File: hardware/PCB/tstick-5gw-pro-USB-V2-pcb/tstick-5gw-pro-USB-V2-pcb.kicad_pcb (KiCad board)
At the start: 4 copper layers, 53.3 x 25.4 mm, 62 parts, among them J1 USB_C_Receptacle_USB2.0, Q1 BSS138, Q2 BSS138, Q3 BSS138, SW1 B3U-1000P, SW2 B3U-1000P, U1 USBLC6-2P6, U2 MCP73871, U3 NCP167AMX330TBG, U4 NCP167AMX180TBG

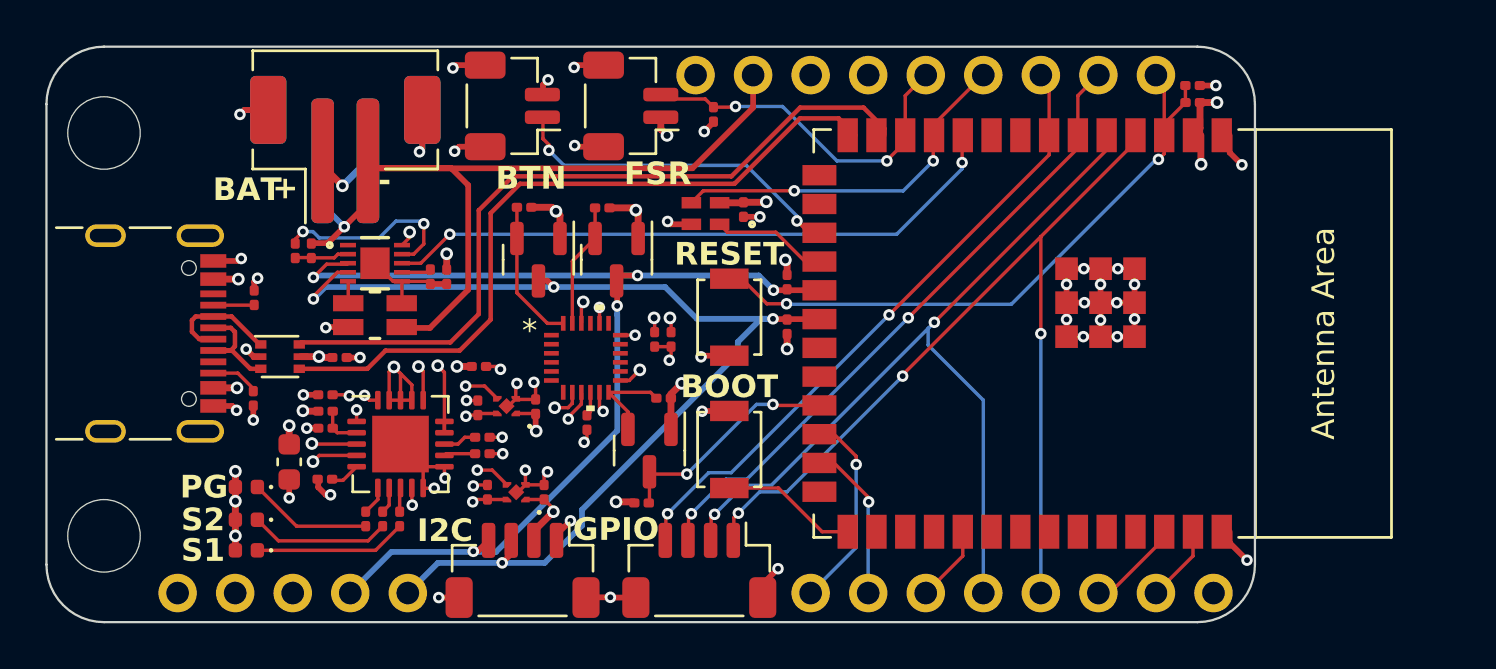
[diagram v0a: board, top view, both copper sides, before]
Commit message: removed neopixel, changed BOM, added simple status LEDs
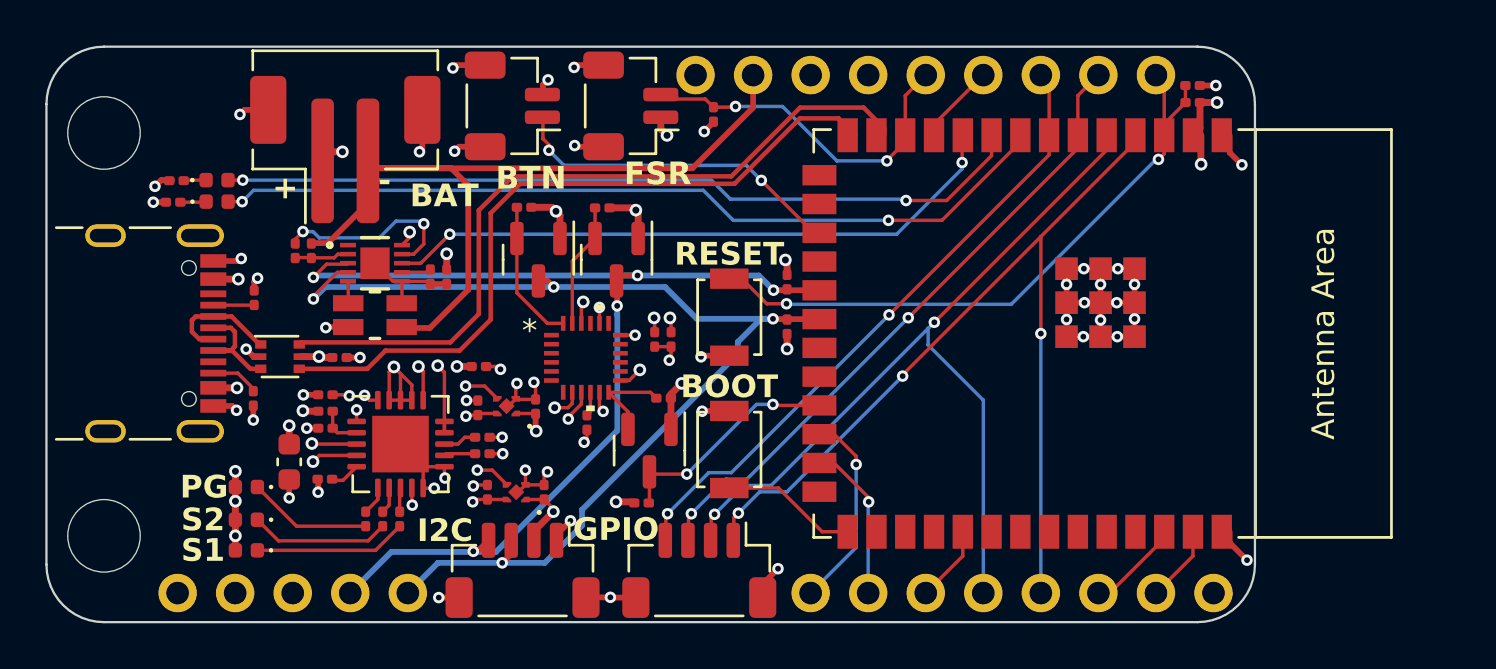
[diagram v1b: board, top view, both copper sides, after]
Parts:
- removed BT2: JST-PH-1x02-2.000mm, Connector_JST:JST_PH_B2B-PH-SM4-TB_1x02-1MP_P2.00mm_Vertical
- removed C13: 0.1uF, Capacitor_SMD:C_0201_0603Metric
- removed PWLED1: SK6805-E-J, neopixel-1515-footprints:4492_ADA
- added R10: 1k, Resistor_SMD:R_0201_0603Metric, F.Cu at (98.5, 54.2)
- added R8: 1k, Resistor_SMD:R_0201_0603Metric, F.Cu at (98.3, 55.1)
- added STATLED1: LED, LED_SMD:LED_0402_1005Metric, F.Cu at (100.2, 55.1)
- added STATLED2: LED, LED_SMD:LED_0402_1005Metric, F.Cu at (100.2, 54.1)
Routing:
- net /IO15: track 0.00 -> 37.5 mm, vias 0 -> 2
- net /IO16: track 0.00 -> 35.8 mm, vias 0 -> 2
- net /IO18: track 16.1 -> 3.56 mm, vias 2 -> 0
- net /IO10: track 6.41 -> 0.00 mm
- net GND: track 72.6 -> 68.5 mm
- net -BATT: track 40.4 -> 37.1 mm, vias 1 -> 0
- net +3V3: track 11.9 -> 9.83 mm, vias 8 -> 7
- net +BATT: track 10.2 -> 8.23 mm
- net Net-(STATLED1-K): track 0.00 -> 1.13 mm
- net Net-(STATLED2-K): track 0.00 -> 0.86 mm
- net /IO9: track 15.5 -> 14.8 mm

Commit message: removed unused fuel gauge thresholds, added jab thresholds
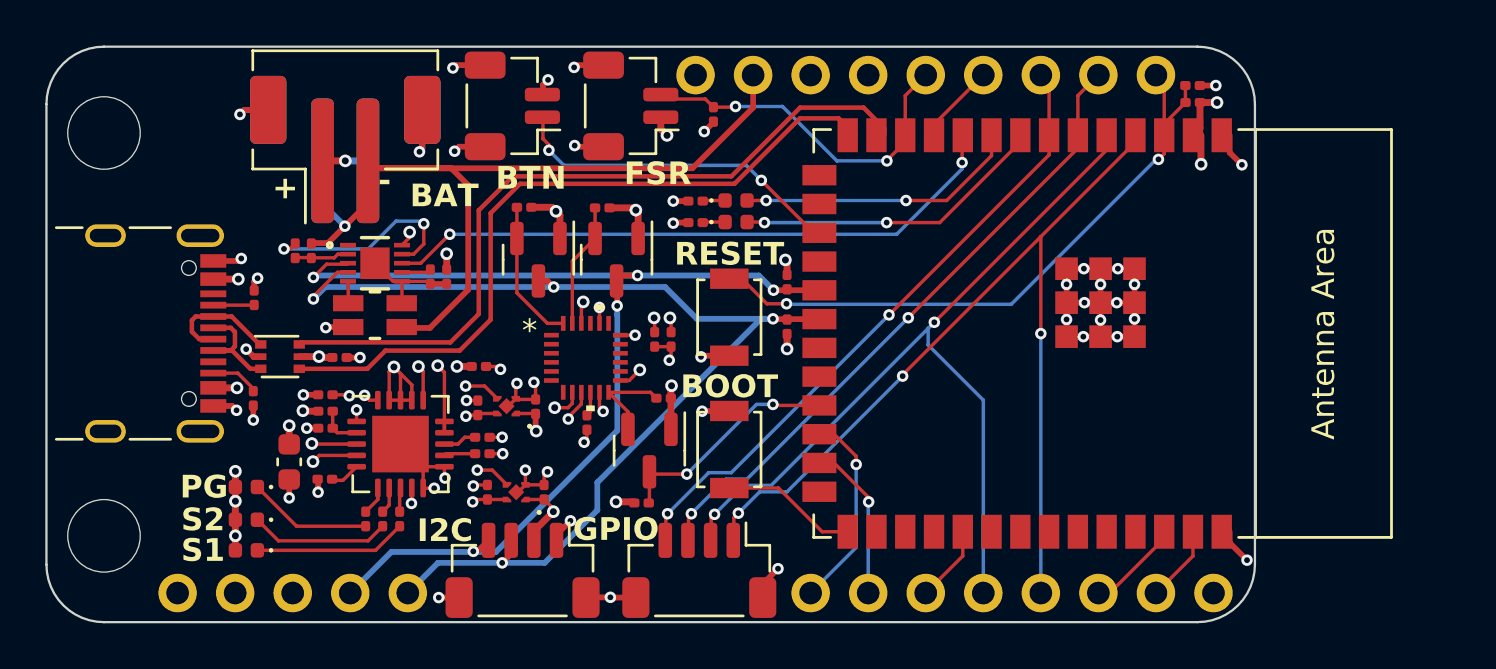
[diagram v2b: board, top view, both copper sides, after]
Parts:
- added BT2: JST-PH-1x02-2.000mm, Connector_JST:JST_PH_B2B-PH-SM4-TB_1x02-1MP_P2.00mm_Vertical, B.Cu at (105.9, 52.8)
- CHARGLED1: value LED -> S1
- CHARGLED2: value LED -> S2
- CHARGLED3: value LED -> PG
- STATLED1: value LED -> WIFISTATUS
- STATLED2: value LED -> GENERAL STATUS
- moved R8 23.1 mm to (121.4, 56.0)
- moved R10 22.9 mm to (121.4, 55.1)
- moved STATLED1 22.9 mm to (123.2, 56.0)
- moved STATLED2 22.9 mm to (123.1, 55.0)
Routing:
- net /IO15: track 37.5 -> 13.8 mm
- net /IO16: track 35.8 -> 12.5 mm
- net -BATT: track 37.1 -> 40.4 mm, vias 0 -> 1
- net GND: track 68.5 -> 71.5 mm
- net +BATT: track 8.23 -> 9.19 mm
- net /THRM: track 8.52 -> 9.37 mm
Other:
- board text added: "FSR IO8"
- board text removed: "FSR IO3"

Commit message: bumped up all package sizes from a minimum of 0201 to 0402
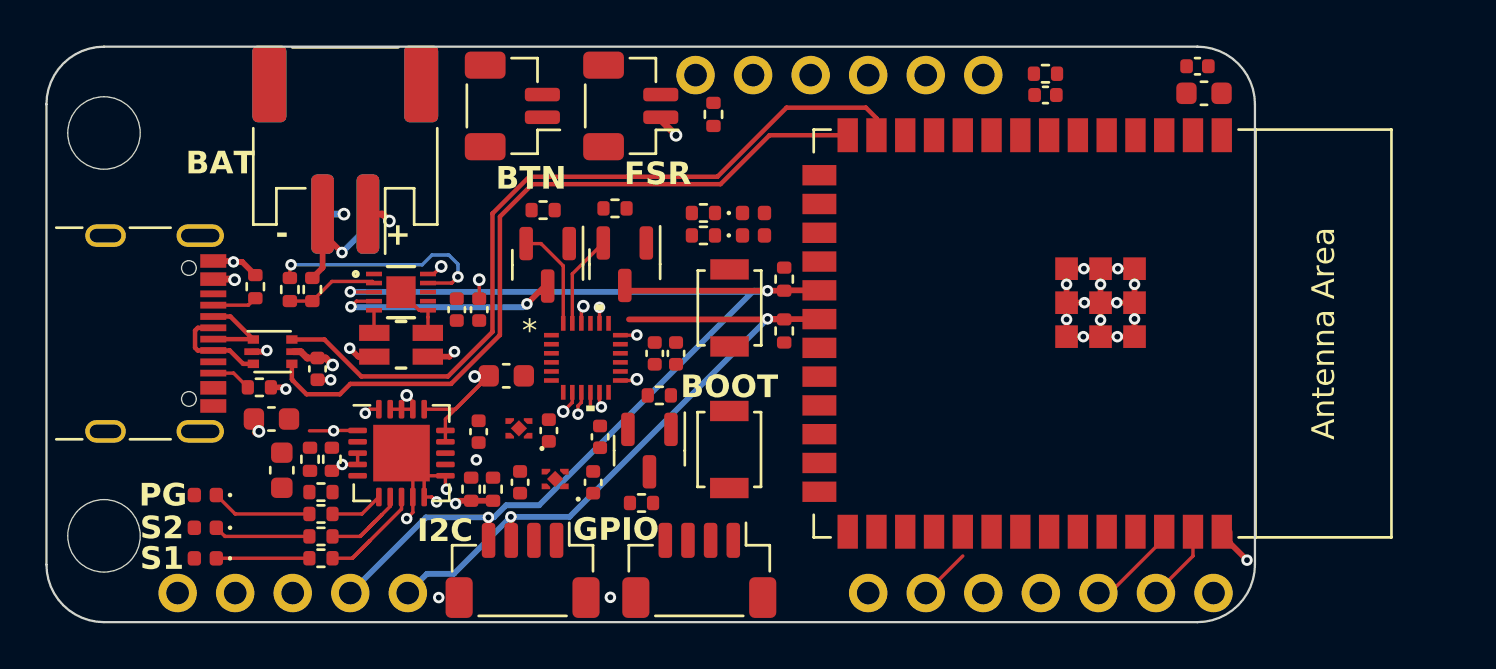
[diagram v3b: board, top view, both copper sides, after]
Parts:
- added C13: 10uF, Capacitor_SMD:C_0603_1608Metric, F.Cu at (143.8, 50.3)
- added C19: 0.1uF, Capacitor_SMD:C_0402_1005Metric, F.Cu at (143.5, 49.1)
- BT1, BT2: footprint Connector_JST:JST_PH_B2B-PH-SM4-TB_1x02-1MP_P2.00mm_Vertical -> Connector_JST:JST_PH_S2B-PH-SM4-TB_1x02-1MP_P2.00mm_Horizontal
- C1, C10, C11, C12, C15, C2, C4, C5, C6, C7, C9: footprint Capacitor_SMD:C_0201_0603Metric -> Capacitor_SMD:C_0402_1005Metric
- C3, C8: footprint Capacitor_SMD:C_0201_0603Metric -> Capacitor_SMD:C_0603_1608Metric
- R1, R10, R12, R14, R15, R16, R17, R18, R19, R20, R21, R22, R23, R24, R3, R4, R5, R6, R7, R8, R9, TH1: footprint Resistor_SMD:R_0201_0603Metric -> Resistor_SMD:R_0402_1005Metric
- moved R5 6.62 mm to (136.8, 49.5), turned to 180 degrees
- moved C9 6.51 mm to (136.8, 50.4), turned to 180 degrees
- moved R3 3.88 mm to (104.8, 70.8), turned to 0 degrees
- moved C3 3.84 mm to (103.1, 67.0), turned to -90 degrees
- moved R22 2.83 mm to (104.8, 69.9), turned to 0 degrees
- moved R20 2.34 mm to (112.4, 67.8), turned to 90 degrees
- moved R18 2.23 mm to (104.3, 66.5), turned to -90 degrees
- moved C5 2.21 mm to (116.8, 67.5)
- moved C14 2.05 mm to (102.6, 64.7), turned to 0 degrees
- moved C1 2.04 mm to (111.8, 59.9)
- moved R24 1.99 mm to (104.8, 68.9), turned to 0 degrees
- moved C2 1.86 mm to (110.8, 59.9)
- moved CHARGLED3 1.85 mm to (99.7, 68.0)
- moved CHARGLED1 1.85 mm to (99.7, 70.8)
- moved CHARGLED2 1.85 mm to (99.7, 69.5)
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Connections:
- BOARDLAYOUT1 pad 10: GND -> /IO8
- BOARDLAYOUT1 pad 11: /IO1 -> /COPI
- BOARDLAYOUT1 pad 12: /IO2 -> /SCK
- BOARDLAYOUT1 pad 13: /IO4 -> /CIPO
- BOARDLAYOUT1 pad 14: /IO5 -> /SDA
- BOARDLAYOUT1 pad 15: /COPI -> /SCL
- BOARDLAYOUT1 pad 16: /SCK -> GND
- BOARDLAYOUT1 pad 17: /CIPO -> +3V3
- BOARDLAYOUT1 pad 18: /SDA -> VUSB
- BOARDLAYOUT1 pad 3: +3V3 -> SYS
- BOARDLAYOUT1 pad 5: /IO8 -> +3V3
- BOARDLAYOUT1 pad 6: /IO18 -> /EN
- BOARDLAYOUT1 pad 7: /IO7 -> GND
- BOARDLAYOUT1 pad 8: /IO6 -> /IO1
- BOARDLAYOUT1 pad 9: /EN -> /IO2
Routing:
- net /IO4: track 41.7 -> 0.00 mm, vias 3 -> 0
- net /IO5: track 38.5 -> 0.00 mm, vias 2 -> 0
- net GND: track 71.5 -> 37.5 mm, vias 60 -> 28
- net /EN: track 28.6 -> 0.00 mm, vias 2 -> 0
- net /IO6: track 28.6 -> 0.00 mm, vias 2 -> 0
- net /IO7: track 28.3 -> 0.00 mm, vias 2 -> 0
- net /IO17: track 28.1 -> 0.00 mm, vias 2 -> 0
- net -BATT: track 40.4 -> 16.0 mm, vias 1 -> 2
- net SYS: track 8.15 -> 31.9 mm, vias 7 -> 3
- net /IO8: track 15.7 -> 0.00 mm, vias 2 -> 0
- net /IO9: track 14.8 -> 0.00 mm, vias 2 -> 0
- net /IO15: track 13.8 -> 0.00 mm, vias 2 -> 0
- net /IO16: track 12.5 -> 0.00 mm, vias 2 -> 0
- net +1V8: track 13.2 -> 2.56 mm, vias 9 -> 3
- net /IO21: track 10.5 -> 0.00 mm, vias 2 -> 0
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
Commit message: finished routing for the new pcb layout, will review later
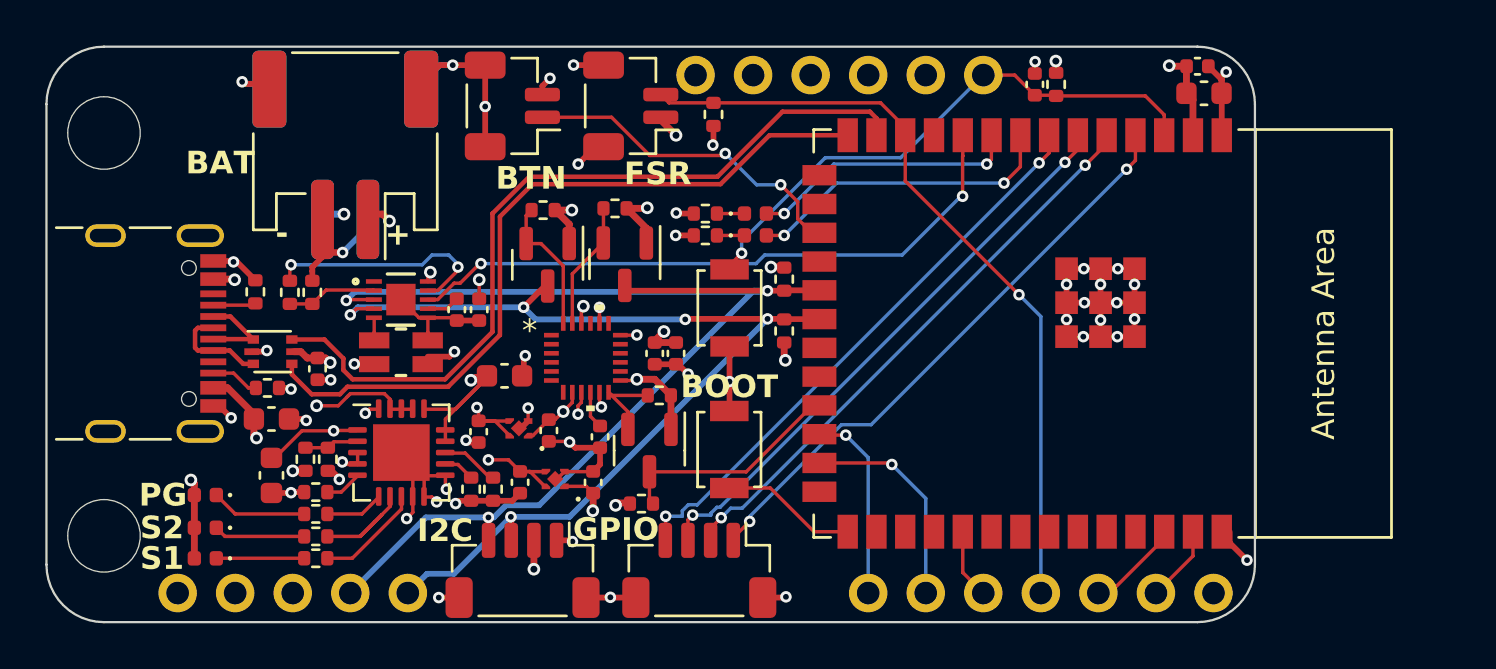
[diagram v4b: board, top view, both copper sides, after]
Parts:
- moved R8 0.99 mm to (121.8, 56.6)
- moved STATLED1 0.99 mm to (124.0, 56.6)
- moved R10 0.97 mm to (121.8, 55.6)
- moved STATLED2 0.97 mm to (124.0, 55.6)
- moved R5 0.66 mm to (137.3, 49.9), turned to 90 degrees
- moved C9 0.66 mm to (136.3, 49.9), turned to 90 degrees
- moved C3 0.51 mm to (102.6, 67.2)
- moved R6 0.36 mm to (102.5, 63.3)
- moved FG1 0.33 mm to (108.4, 59.4)
- moved R2 0.33 mm to (108.4, 61.7)
- moved BT1 0.24 mm to (105.9, 53.0)
- moved BT2 0.24 mm to (105.9, 53.0)
- moved R22 0.23 mm to (104.6, 69.9)
- moved R24 0.23 mm to (104.6, 68.9)
- moved R3 0.23 mm to (104.6, 70.8)
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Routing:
- net GND: track 37.5 -> 81.5 mm, vias 28 -> 51
- net /IO8: track 0.00 -> 34.4 mm, vias 0 -> 1
- net /IO17: track 0.00 -> 28.2 mm, vias 0 -> 2
- net /IO4: track 0.00 -> 26.0 mm, vias 0 -> 2
- net /IO7: track 0.00 -> 25.6 mm, vias 0 -> 2
- net /IO6: track 0.00 -> 25.6 mm, vias 0 -> 2
- net /IO5: track 0.00 -> 25.4 mm, vias 0 -> 2
- net /EN: track 0.00 -> 24.7 mm, vias 0 -> 1
- net -BATT: track 16.0 -> 35.4 mm
- net /IO9: track 0.00 -> 14.9 mm, vias 0 -> 2
- net /IO15: track 0.00 -> 13.9 mm, vias 0 -> 2
- net +1V8: track 2.56 -> 14.8 mm, vias 3 -> 6
- net /IO16: track 0.00 -> 12.0 mm, vias 0 -> 2
- net /IO21: track 0.00 -> 10.2 mm
- net +3V3: track 1.08 -> 11.1 mm, vias 1 -> 8
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
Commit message: finished verifying pcb routing, updated pcb silkscreen
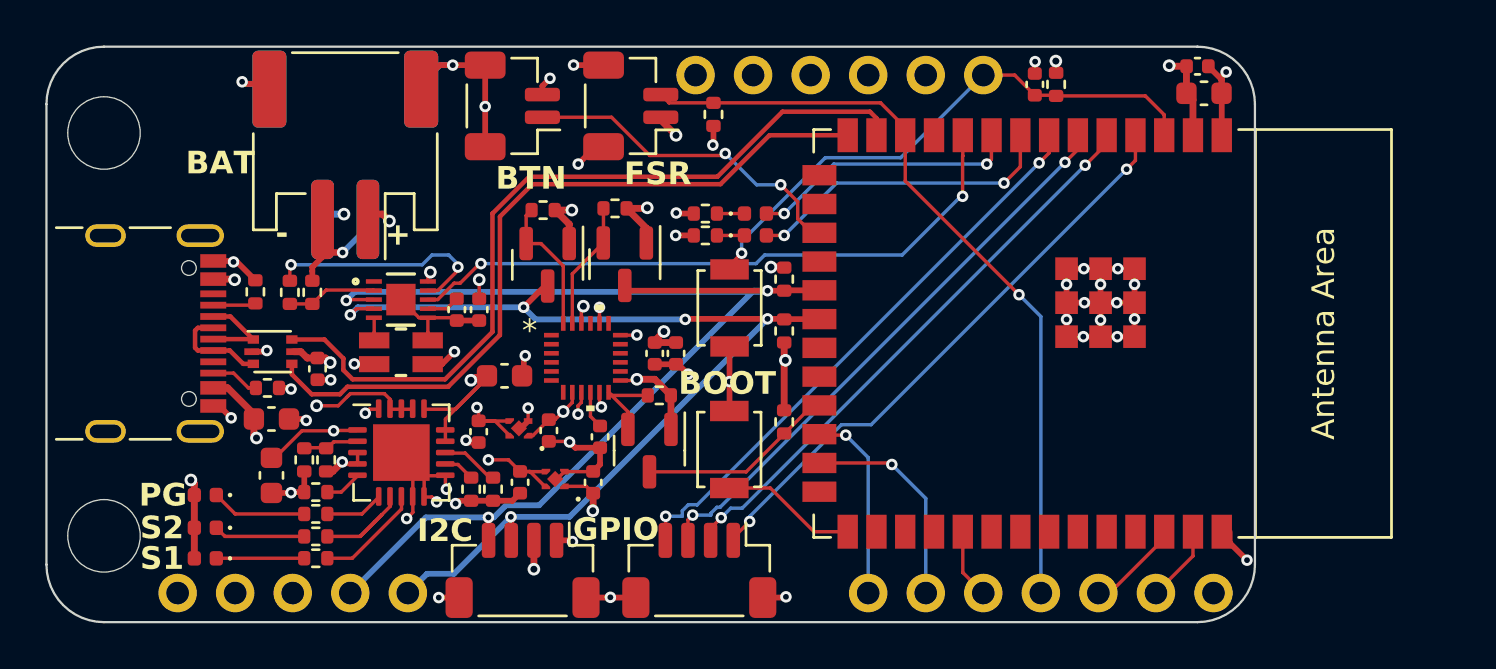
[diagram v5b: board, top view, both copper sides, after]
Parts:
- moved R23 7.26 mm to (125.3, 64.8), turned to 90 degrees
- moved R4 1.04 mm to (104.1, 66.5)
- moved R18 0.91 mm to (105.1, 66.5)
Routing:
- net +3V3: track 11.1 -> 12.6 mm, vias 8 -> 7
- net /IO21: track 10.2 -> 8.71 mm
- net GND: track 81.5 -> 81.9 mm, vias 51 -> 50
- net VUSB: track 21.0 -> 21.4 mm, vias 7 -> 6
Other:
- board text added: "EnchantiS3 v0.1 2023-12 IDMIL McGill University Albert Niyonsenga"
- board text removed: "Custom T-Stick Board v1.1 2023-11 IDMIL McGill University Albert Niyonsenga"

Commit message: moved LEDs, to the front of the board, took new screenshots
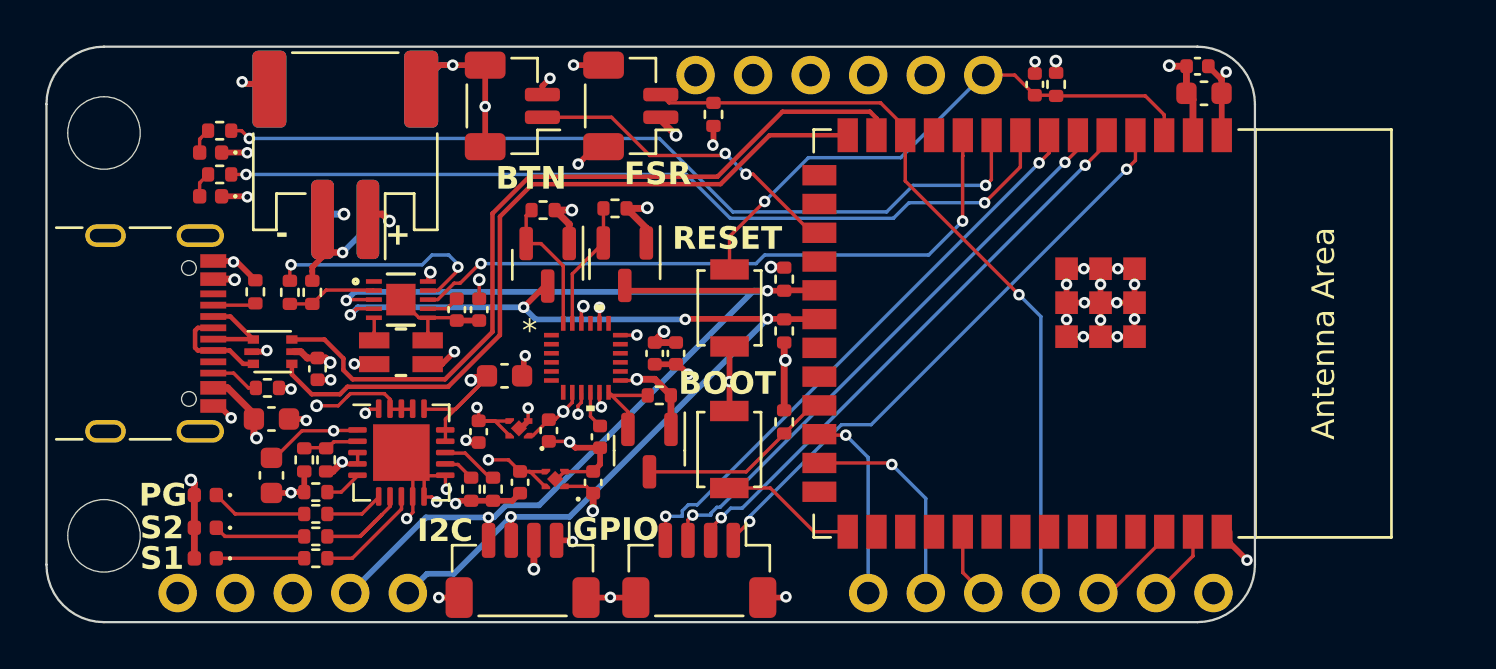
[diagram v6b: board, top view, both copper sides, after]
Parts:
- moved STATLED2 24.2 mm to (100.0, 52.9), turned to 180 degrees
- moved STATLED1 24.1 mm to (100.0, 54.9), turned to 180 degrees
- moved R10 21.7 mm to (100.4, 52.0)
- moved R8 21.6 mm to (100.4, 53.9)
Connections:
- R10 pad 1: Net-(STATLED2-K) -> /IO16
- R10 pad 2: GND -> Net-(STATLED2-A)
- R8 pad 1: Net-(STATLED1-K) -> /IO15
- R8 pad 2: GND -> Net-(STATLED1-A)
- STATLED1 pad 1: Net-(STATLED1-K) -> GND
- STATLED1 pad 2: /IO15 -> Net-(STATLED1-A)
- STATLED2 pad 1: Net-(STATLED2-K) -> GND
- STATLED2 pad 2: /IO16 -> Net-(STATLED2-A)
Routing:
- net /IO16: track 12.0 -> 37.6 mm
- net /IO15: track 13.9 -> 38.0 mm
- net Net-(STATLED2-K): track 1.21 -> 0.00 mm
- net Net-(STATLED1-K): track 1.21 -> 0.00 mm
- net Net-(STATLED2-A): track 0.00 -> 1.12 mm
- net Net-(STATLED1-A): track 0.00 -> 1.12 mm
- net GND: track 81.9 -> 82.7 mm
- net /IO17: track 28.2 -> 28.8 mm
